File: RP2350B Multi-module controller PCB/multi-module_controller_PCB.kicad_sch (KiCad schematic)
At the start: 79 parts, among them J2 Conn_02x26_Odd_Even, J3 Conn_02x26_Odd_Even, J4 SM03B-SRSS-TB, J5 USB_C_Receptacle_USB2.0_14P, J6 USB_C_Receptacle_USB2.0_14P, J7 Module_Bay, J8 USB_A, SW1 SW_Push, SW10 BTN_MDL, SW2 SW_Push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

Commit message: all core components placed and routed
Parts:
- C11, C12, C13, C14, C15, C16, C17, C18, C2, C20, C21, C23, C8: LCSC C157353 -> (none)
- C24: LCSC C140782 -> (none)
- J2, J3: now not fitted
- J5, J6: footprint (none) -> Connector_USB:USB_C_Receptacle_G-Switch_GT-USB-7010ASV
- J7: footprint (none) -> Connector_PinHeader_2.54mm:PinHeader_1x08_P2.54mm_Vertical
- J8: footprint (none) -> Connector_USB:USB_A_Connfly_DS1095
- U1: LCSC C42415655 -> (none)
- U2: LCSC C88234 -> (none)
- U3: LCSC C97521 -> (none)
- U5: LCSC C11355 -> (none)
- U6: LCSC C144190 -> (none)
- Y1: LCSC C20625731 -> (none)
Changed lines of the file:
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@@
 			)
 		)
-		(property "LCSC" "C97521"
-			(at 60.96 90.805 0)
-			(effects
-				(font
-					(size 1.27 1.27)
-				)
-				(hide yes)
-			)
-		)
 		(pin "1"
 		)
@@
 			)
 		)
-		(property "LCSC" "C157353"
-			(at 79.121 82.0166 0)
-			(effects
-				(font
-					(size 1.27 1.27)
-				)
-				(hide yes)
-			)
-		)
 		(pin "1"
 		)
@@
 			)
 		)
-		(property "LCSC" "C157353"
-			(at 255.651 30.5816 0)
-			(effects
-				(font
-					(size 1.27 1.27)
-				)
-				(hide yes)
-			)
-		)
 		(pin "1"
 		)
@@
 			)
 		)
-		(property "LCSC" "C157353"
-			(at 267.081 30.5816 0)
-			(effects
-				(font
-					(size 1.27 1.27)
-				)
-				(hide yes)
-			)
-		)
 		(pin "1"
 		)
@@
 			)
 		)
-		(property "LCSC" "C157353"
-			(at 278.511 30.5816 0)
-			(effects
-				(font
-					(size 1.27 1.27)
-				)
-				(hide yes)
-			)
-		)
 		(pin "1"
 		)
@@
 			)
 		)
-		(property "LCSC" "C157353"
-			(at 289.941 30.5816 0)
-			(effects
-				(font
-					(size 1.27 1.27)
-				)
-				(hide yes)
-			)
-		)
 		(pin "1"
 		)
@@
 			)
 		)
-		(property "LCSC" "C157353"
-			(at 301.371 30.5816 0)
-			(effects
-				(font
-					(size 1.27 1.27)
-				)
-				(hide yes)
-			)
-		)
 		(pin "1"
 		)
@@
 			)
 		)
-		(property "LCSC" "C157353"
-			(at 312.801 30.5816 0)
-			(effects
-				(font
-					(size 1.27 1.27)
-				)
-				(hide yes)
-			)
-		)
 		(pin "1"
 		)
@@
 			)
 		)
-		(property "LCSC" "C88234"
-			(at 82.55 21.7932 0)
-			(effects
-				(font
-					(size 1.27 1.27)
-				)
-				(hide yes)
-			)
-		)
 		(pin "1"
 		)
@@
 			)
 		)
-		(property "LCSC" "C20625731"
-			(at 82.55 188.595 0)
-			(effects
-				(font
-					(size 1.27 1.27)
-				)
-				(hide yes)
-			)
-		)
 		(pin "1"
 		)
@@
 		(in_bom yes)
 		(on_board yes)
-		(dnp no)
+		(dnp yes)
 		(property "Reference" "J3"
 			(at 391.16 83.82 0)
@@
 		(in_bom yes)
 		(on_board yes)
-		(dnp no)
+		(dnp yes)
 		(property "Reference" "J2"
 			(at 334.01 83.82 0)
@@
 			)
 		)
-		(property "LCSC" "C140782"
-			(at 56.1721 257.8741 0)
-			(effects
-				(font
-					(size 1.27 1.27)
-				)
-				(hide yes)
-			)
-		)
 		(pin "1"
 		)
@@
 			)
 		)
-		(property "LCSC" "C157353"
-			(at 170.561 30.5816 0)
-			(effects
-				(font
-					(size 1.27 1.27)
-				)
-				(hide yes)
-			)
-		)
 		(pin "1"
 		)
@@
 			)
 		)
-		(property "LCSC" "C157353"
-			(at 244.221 30.5816 0)
-			(effects
-				(font
-					(size 1.27 1.27)
-				)
-				(hide yes)
-			)
-		)
 		(pin "1"
 		)
@@
 			)
 		)
-		(property "LCSC" "C11355"
-			(at 130.4133 218.1055 0)
-			(effects
-				(font
-					(size 1.27 1.27)
-				)
-				(hide yes)
-			)
-		)
 		(pin "7"
 		)
@@
 			)
 		)
-		(property "LCSC" "C157353"
-			(at 324.231 30.5816 0)
-			(effects
-				(font
-					(size 1.27 1.27)
-				)
-				(hide yes)
-			)
-		)
 		(pin "1"
 		)
@@
 			)
 		)
-		(property "LCSC" "C157353"
-			(at 50.0761 257.6201 0)
-			(effects
-				(font
-					(size 1.27 1.27)
-				)
-				(hide yes)
-			)
-		)
 		(pin "1"
 		)
@@
 			)
 		)
-		(property "Footprint" ""
+		(property "Footprint" "Connector_USB:USB_C_Receptacle_G-Switch_GT-USB-7010ASV"
 			(at 181.61 257.81 0)
 			(effects
@@
 			)
 		)
-		(property "LCSC" "C144190"
-			(at 104.14 244.7755 0)
-			(effects
-				(font
-					(size 1.27 1.27)
-				)
-				(hide yes)
-			)
-		)
 		(pin "2"
 		)
@@
 			)
 		)
-		(property "Footprint" ""
+		(property "Footprint" "Connector_PinHeader_2.54mm:PinHeader_1x08_P2.54mm_Vertical"
 			(at 25.4 262.89 0)
 			(effects
@@
 			)
 		)
-		(property "LCSC" "C157353"
-			(at 147.701 30.5816 0)
-			(effects
-				(font
-					(size 1.27 1.27)
-				)
-				(hide yes)
-			)
-		)
 		(pin "1"
 		)
@@
 			)
 		)
-		(property "LCSC" "C157353"
-			(at 232.156 30.5816 0)
-			(effects
-				(font
-					(size 1.27 1.27)
-				)
-				(hide yes)
-			)
-		)
 		(pin "1"
 		)
@@
 			)
 		)
-		(property "Footprint" ""
+		(property "Footprint" "Connector_USB:USB_A_Connfly_DS1095"
 			(at 151.13 215.9 0)
 			(effects
@@
 			)
 		)
-		(property "LCSC" "C42415655"
-			(at 201.5841 207.01 0)
-			(effects
-				(font
-					(size 1.27 1.27)
-				)
-				(hide yes)
-			)
-		)
 		(pin "1"
 		)
@@
 			)
 		)
-		(property "Footprint" ""
+		(property "Footprint" "Connector_USB:USB_C_Receptacle_G-Switch_GT-USB-7010ASV"
 			(at 33.02 38.1 0)
 			(effects

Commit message: completed layout, include production files, before adjusting component mounting
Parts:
- added J1: Conn_02x06_Odd_Even, Connector_PinSocket_2.54mm:PinSocket_2x06_P2.54mm_Vertical, symbol Connector_Generic:Conn_02x06_Odd_Even
- added J9: ADC_Breakout, Connector_JST:JST_PH_B12B-PH-K_1x12_P2.00mm_Vertical, symbol Connector_Generic:Conn_01x12
- C1, C19, C5: LCSC (none) -> C15850
- C10, C6, C7, C9: LCSC (none) -> C23733
- C11, C12, C13, C14, C15, C16, C17, C18, C2, C20, C21, C23, C25, C8: LCSC (none) -> C1525
- C24: footprint Capacitor_SMD:C_0603_1608Metric -> Capacitor_SMD:C_0805_2012Metric; LCSC (none) -> C16780
- C3, C4: LCSC (none) -> C7467172
- J4: footprint Connector_JST:JST_SH_SM03B-SRSS-TB_1x03-1MP_P1.00mm_Horizontal -> Connector_PinHeader_2.54mm:PinHeader_1x03_P2.54mm_Vertical; symbol Connector_Generic_MountingPin:Conn_01x03_MountingPin -> Connector_Generic:Conn_01x03
- J5, J6: LCSC (none) -> C2988369
- J7: LCSC (none) -> C19184340
- J8: LCSC (none) -> C456018
- L1: LCSC (none) -> C42411119
- R10: LCSC (none) -> C17168
- R12, R5: LCSC (none) -> C25905
- R14, R18: LCSC (none) -> C25744
- R15, R16: value R -> 10k; footprint (none) -> Resistor_SMD:R_0402_1005Metric; LCSC (none) -> C25744
- R17, R19: LCSC (none) -> C25792
- R2, R4, R6: LCSC (none) -> C11702
- R20: LCSC (none) -> C25130
- R21, R22: LCSC (none) -> C25104
- R23, R24: LCSC (none) -> C2906875
- R3: LCSC (none) -> C25105
- R7, R8: LCSC (none) -> C25100
- SW1, SW2: LCSC (none) -> C2910644
- SW10, SW3, SW4, SW5, SW6, SW7, SW8, SW9: LCSC (none) -> C2837532
- U1: LCSC (none) -> C42415655
- U2: LCSC (none) -> C88234
- U3: LCSC (none) -> C97521
- U5: LCSC (none) -> C11355
- U6: LCSC (none) -> C144190
- Y1: LCSC (none) -> C20625731
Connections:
- net +3V3: now also J1.10 (Pin_10), J1.12 (Pin_12), J1.8 (Pin_8), J9.1 (Pin_1)
- net GND: now also J1.1 (Pin_1), J1.11 (Pin_11), J1.3 (Pin_3), J1.5 (Pin_5), J1.7 (Pin_7), J1.9 (Pin_9), J9.3 (Pin_3), J9.4 (Pin_4); no longer J4.MP (MountPin)
- net GPIO40_ADC0: now also J9.12 (Pin_12); no longer J3.15 (Pin_15)
- net GPIO41_ADC1: now also J9.11 (Pin_11); no longer J3.13 (Pin_13)
- net GPIO42_ADC2: now also J9.10 (Pin_10); no longer J3.11 (Pin_11)
- net GPIO43_ADC3: now also J9.9 (Pin_9); no longer J3.9 (Pin_9)
- net GPIO44_ADC4: now also J9.8 (Pin_8); no longer J3.7 (Pin_7)
- net GPIO45_ADC5: now also J9.7 (Pin_7); no longer J3.5 (Pin_5)
- net GPIO46_ADC6: now also J9.6 (Pin_6); no longer J3.3 (Pin_3)
- net GPIO47_ADC7: now also J9.5 (Pin_5); no longer J3.1 (Pin_1)
- net VBUS: now also J1.2 (Pin_2), J1.4 (Pin_4), J1.6 (Pin_6), J9.2 (Pin_2)
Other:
- note added: "SWD Debug Connector"
- note removed: "JST Debug Connector"

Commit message: adjust GPIO breakout, add LED, silkscreen labels, etc
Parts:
- removed J9: ADC_Breakout, Connector_JST:JST_PH_B12B-PH-K_1x12_P2.00mm_Vertical, symbol Connector_Generic:Conn_01x12
- added D1: LED, LED_SMD:LED_0603_1608Metric, symbol Device:LED
- added J10: Internal unused GPIO Breakout, Connector_PinHeader_1.27mm:PinHeader_2x03_P1.27mm_Vertical, symbol Connector_Generic:Conn_02x03_Odd_Even
- added J9: ADC_Breakout, Connector_PinHeader_2.54mm:PinHeader_2x09_P2.54mm_Vertical, symbol Connector_Generic:Conn_02x09_Odd_Even
- added R25: 220, Resistor_SMD:R_0603_1608Metric, symbol Device:R
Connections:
- net +3V3: now also J9.1 (Pin_1)
- net GND: now also D1.1 (K), J10.1 (Pin_1), J9.3 (Pin_3), J9.4 (Pin_4)
- net GPIO17: now also J10.3 (Pin_3); no longer J2.38 (Pin_38)
- net GPIO18: now also J10.2 (Pin_2); no longer J2.40 (Pin_40)
- net GPIO19: now also J10.4 (Pin_4); no longer J2.42 (Pin_42)
- net GPIO20: now also J10.6 (Pin_6); no longer J2.44 (Pin_44)
- net GPIO21: now also J10.5 (Pin_5); no longer J2.46 (Pin_46)
- net GPIO33: now also R25.1; no longer J3.29 (Pin_29)
- net GPIO34: now also J9.17 (Pin_17); no longer J3.27 (Pin_27)
- net GPIO35: now also J9.18 (Pin_18); no longer J3.25 (Pin_25)
- net GPIO36: now also J9.15 (Pin_15); no longer J3.23 (Pin_23)
- net GPIO37: now also J9.16 (Pin_16); no longer J3.21 (Pin_21)
- net GPIO38: now also J9.13 (Pin_13); no longer J3.19 (Pin_19)
- net GPIO39: now also J9.14 (Pin_14); no longer J3.17 (Pin_17)
- net GPIO40_ADC0: now also J9.11 (Pin_11)
- net GPIO41_ADC1: now also J9.12 (Pin_12)
- net GPIO42_ADC2: now also J9.9 (Pin_9)
- net GPIO43_ADC3: now also J9.10 (Pin_10)
- net GPIO44_ADC4: now also J9.7 (Pin_7)
- net GPIO45_ADC5: now also J9.8 (Pin_8)
- net GPIO46_ADC6: now also J9.5 (Pin_5)
- net GPIO47_ADC7: now also J9.6 (Pin_6)
- net VBUS: now also J9.2 (Pin_2)
- new net: D1.2 (A), R25.2
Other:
- note added: "Status LED"
- moved on the sheet: C2, C3, C4, R1, R10, R11, R13, R2, R9, U3, Y1

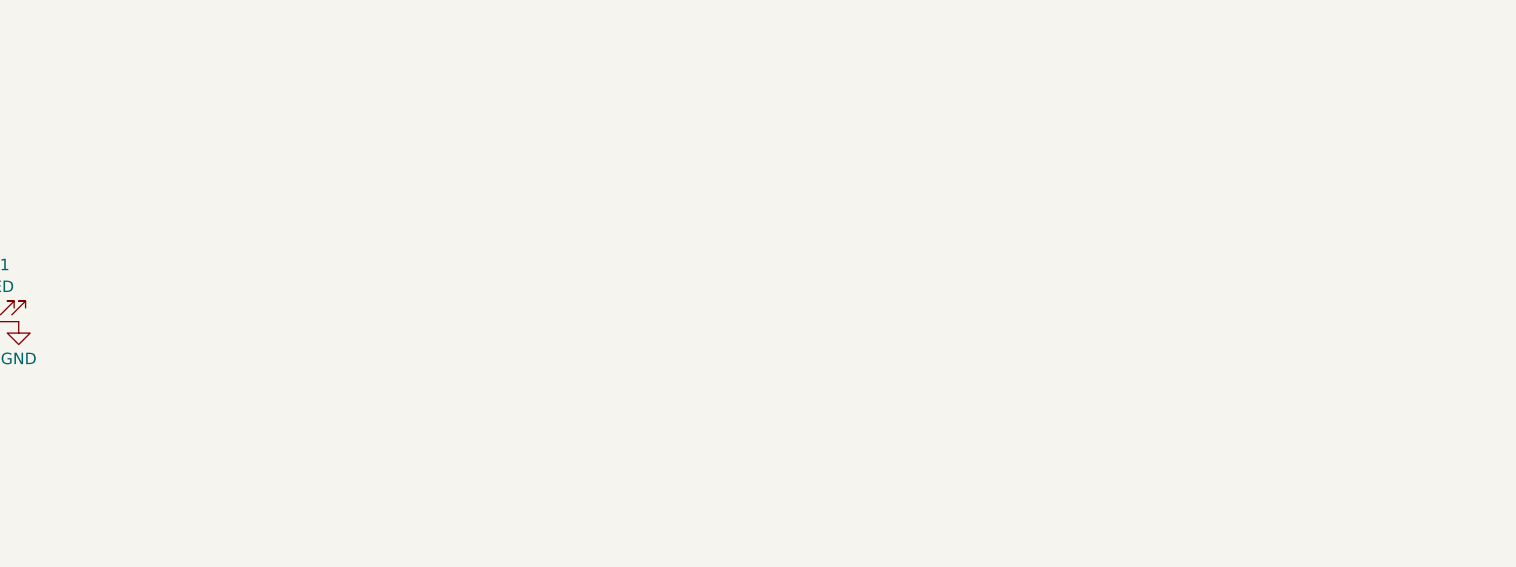
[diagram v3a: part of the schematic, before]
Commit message: add hardware tests for new board
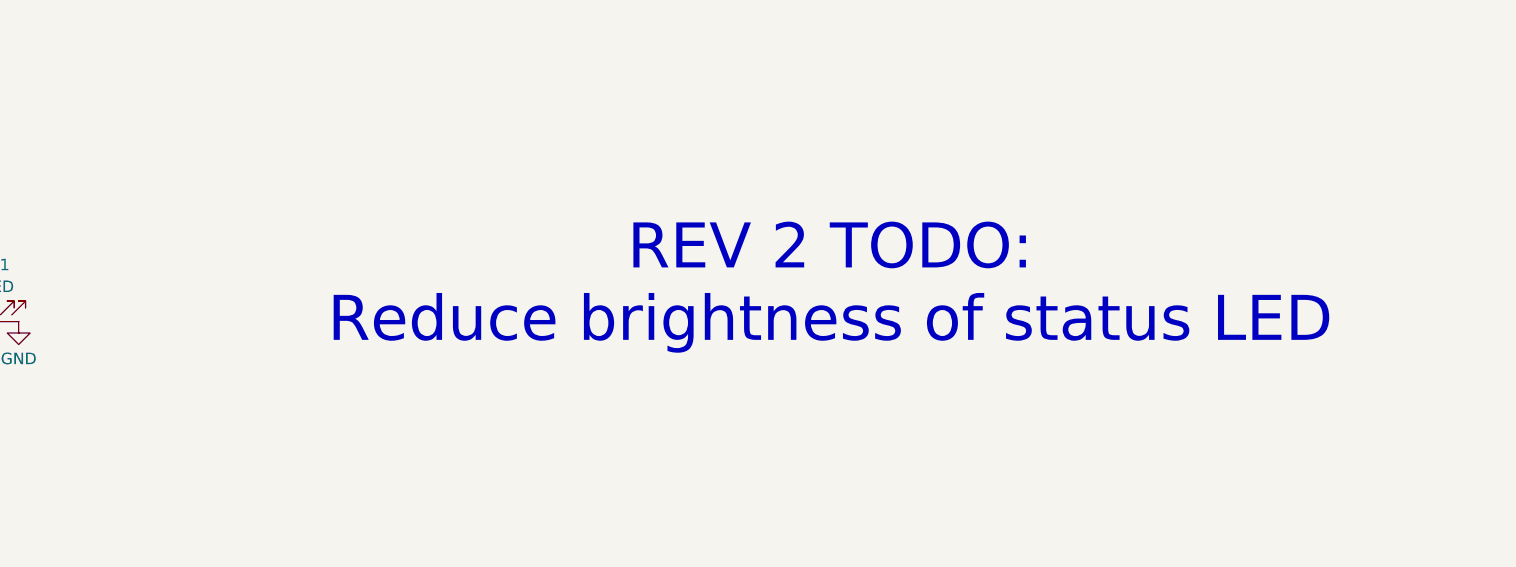
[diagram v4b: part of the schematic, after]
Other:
- note added: "REV 2 TODO: Reduce brightness of status LED"
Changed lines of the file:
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@@
+		)
+	)
+	(text "REV 2 TODO:\nReduce brightness of status LED"
+		(exclude_from_sim no)
+		(at 487.68 238.506 0)
+		(effects
+			(font
+				(size 5 5)
+			)
 		)
 	)

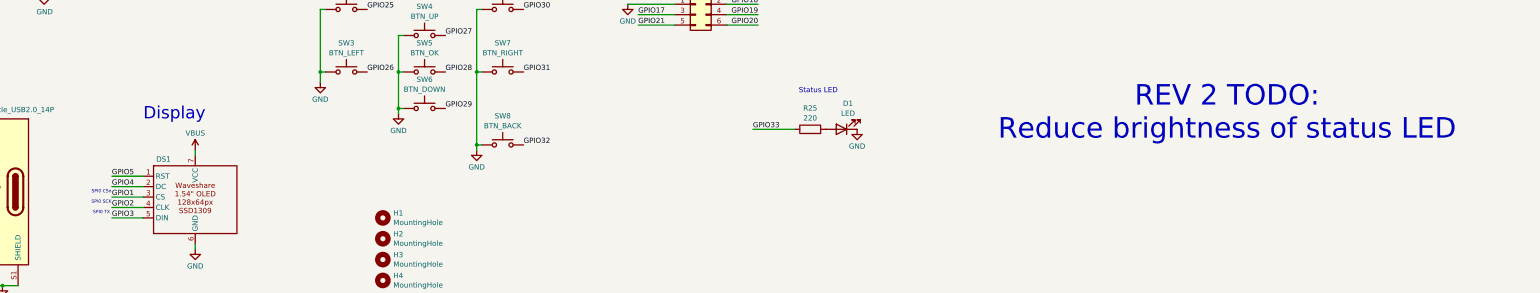
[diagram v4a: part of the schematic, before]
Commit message: Implement pin-remapping and adjustments for new PCB, add support for both USB A and C ports (configured at compile-time by active_usb_port for now). Buttons, i2c display, USB A, USB C, all functional. Multi-module adjustments WIP
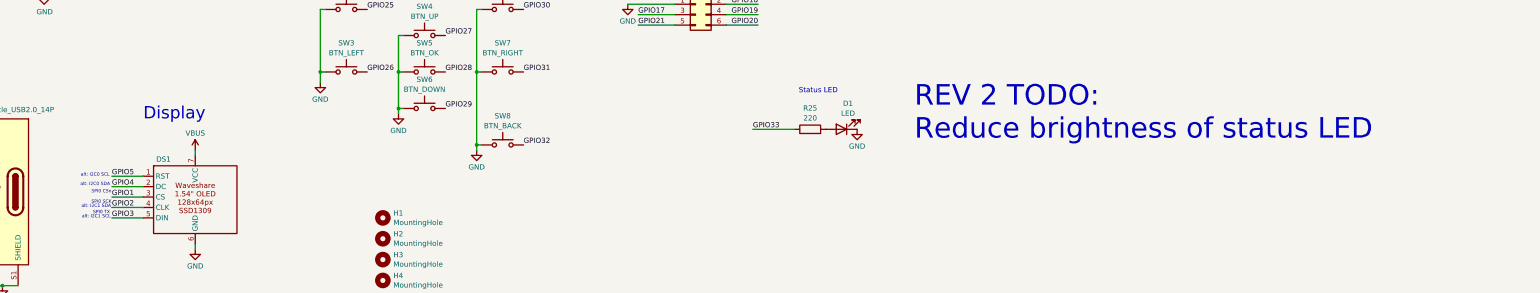
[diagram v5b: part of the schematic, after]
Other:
- note added: "alt: I2C0 SCL"
- note added: "alt: I2C0 SDA"
- note added: "alt: I2C1 SCL"
- note added: "alt: I2C1 SDA"
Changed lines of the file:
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@@
 	(text "REV 2 TODO:\nReduce brightness of status LED"
 		(exclude_from_sim no)
-		(at 487.68 238.506 0)
+		(at 411.48 238.506 0)
 		(effects
 			(font
 				(size 5 5)
 			)
+			(justify left)
 		)
 	)
@@
 		)
 	)
+	(text "alt: I2C0 SCL"
+		(exclude_from_sim no)
+		(at 211.836 253.746 0)
+		(effects
+			(font
+				(size 0.8 0.8)
+			)
+		)
+	)
 	(text "UART0 TX (CSRF)"
 		(exclude_from_sim no)
@@
 		)
 	)
+	(text "alt: I2C1 SCL"
+		(exclude_from_sim no)
+		(at 212.09 263.906 0)
+		(effects
+			(font
+				(size 0.8 0.8)
+			)
+		)
+	)
 	(text "USB Downstream ports"
 		(exclude_from_sim no)
@@
 		)
 	)
+	(text "alt: I2C0 SDA"
+		(exclude_from_sim no)
+		(at 211.836 256.032 0)
+		(effects
+			(font
+				(size 0.8 0.8)
+			)
+		)
+	)
 	(text "UART0 RX"
 		(exclude_from_sim no)
@@
 		(effects
 			(font
+				(size 0.8 0.8)
+			)
+		)
+	)
+	(text "alt: I2C1 SDA"
+		(exclude_from_sim no)
+		(at 212.09 261.366 0)
+		(effects
+			(font

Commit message: start on revisions for REV2 board design
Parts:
- added R26: 22, Resistor_SMD:R_0402_1005Metric, symbol Device:R_Small
- R20: value 680 -> 22
- R21, R22: value 330 -> 22
- R25: value 220 -> 470
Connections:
- net GPIO13: now also R26.2; no longer J7.1 (Pin_1), R20.1
- new net: J7.1 (Pin_1), R20.1, R26.1
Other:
- note added: "REV 2 Changes: Reduce R22, R21, and R20 from 330Ω (or 680Ω) to 22Ω, improving signal response time Add R26 protection resistor Increase R25 from 220Ω to 470Ω to reduce LED brightness"
- note added: "REV 2 TODO: Consider always-on power to USB C CC pins - use ADC to detect downstream devices and auto-switch active port"
- note removed: "REV 2 TODO: Reduce brightness of status LED"
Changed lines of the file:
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@@
 		(title "RP2350B QFN80 Mulit-module controller")
 		(date "2025-12-03")
-		(rev "REV1")
+		(rev "REV2")
 		(company "Patronics and Reject Robotics")
 	)
@@
 		)
 	)
-	(text "REV 2 TODO:\nReduce brightness of status LED"
+	(text "REV 2 TODO:\nConsider always-on power to USB C CC pins\n- use ADC to detect downstream devices and auto-switch active port"
 		(exclude_from_sim no)
-		(at 411.48 238.506 0)
+		(at 43.942 312.928 0)
 		(effects
 			(font
@@
 		)
 	)
+	(text "REV 2 Changes:\nReduce R22, R21, and R20 from 330Ω (or 680Ω) to 22Ω, improving signal response time\nAdd R26 protection resistor\nIncrease R25 from 220Ω to 470Ω to reduce LED brightness"
+		(exclude_from_sim no)
+		(at 40.132 348.996 0)
+		(effects
+			(font
+				(size 5 5)
+			)
+			(justify left)
+		)
+	)
 	(text "USB Downstream ports"
 		(exclude_from_sim no)
@@
 	(wire
 		(pts
-			(xy 45.72 256.54) (xy 30.48 256.54)
+			(xy 236.22 151.13) (xy 251.46 151.13)
 		)
 		(stroke
@@
 	(wire
 		(pts
-			(xy 236.22 151.13) (xy 251.46 151.13)
+			(xy 326.39 104.14) (xy 326.39 106.68)
 		)
 		(stroke
@@
 	(wire
 		(pts
-			(xy 326.39 104.14) (xy 326.39 106.68)
+			(xy 38.1 256.54) (xy 45.72 256.54)
 		)
 		(stroke
@@
 	(wire
 		(pts
+			(xy 30.48 256.54) (xy 33.02 256.54)
+		)
+		(stroke
+			(width 0)
+			(type default)
+		)
+	)
+	(wire
+		(pts
 			(xy 76.2 130.81) (xy 76.2 129.54)
 		)
@@
 			)
 		)
-		(property "Value" "330"
+		(property "Value" "22"
 			(at 35.56 265.0052 90)
 			(effects
@@
 			)
 		)
-		(property "Value" "220"
+		(property "Value" "470"
 			(at 386.08 239.8338 90)
 			(effects
@@
 			)
 		)
-		(property "Value" "330"
+		(property "Value" "22"
 			(at 35.306 261.1952 90)
 			(effects
@@
 	)
 	(symbol
+		(lib_id "Device:R_Small")
+		(at 35.56 256.54 90)
+		(unit 1)
+		(exclude_from_sim no)
+		(in_bom yes)
+		(on_board yes)
+		(dnp no)
+		(property "Reference" "R26"
+			(at 35.56 256.4353 90)
+			(effects
+				(font
+					(size 1.016 1.016)
+				)
+			)
+		)
+		(property "Value" "22"
+			(at 32.766 255.6072 90)
+			(effects
+				(font
+					(size 1.27 1.27)
+				)
+			)
+		)
+		(property "Footprint" "Resistor_SMD:R_0402_1005Metric"
+			(at 35.56 256.54 0)
+			(effects
+				(font
+					(size 1.27 1.27)
+				)
+				(hide yes)
+			)
+		)
+		(property "Datasheet" "~"
+			(at 35.56 256.54 0)
+			(effects
+				(font
+					(size 1.27 1.27)
+				)
+				(hide yes)
+			)
+		)
+		(property "Description" "Resistor, small symbol"
+			(at 35.56 256.54 0)
+			(effects
+				(font
+					(size 1.27 1.27)
+				)
+				(hide yes)
+			)
+		)
+		(property "LCSC" "C25130"
+			(at 35.56 251.8633 0)
+			(effects
+				(font
+					(size 1.27 1.27)
+				)
+				(hide yes)
+			)
+		)
+		(pin "1"
+		)
+		(pin "2"
+		)
+		(instances
+			(project "multi-module_controller_PCB"
+				(path "/94683f5c-9cd9-448e-be96-9792537b5cb8"
+					(reference "R26")
+					(unit 1)
+				)
+			)
+		)
+	)
+	(symbol
 		(lib_id "power:GND")
 		(at 321.31 40.64 0)
@@
 		(on_board yes)
 		(dnp no)
-		(fields_autoplaced yes)
 		(property "Reference" "R20"
-			(at 35.56 249.3233 90)
+			(at 35.56 253.8953 90)
 			(effects
 				(font
@@
 			)
 		)
-		(property "Value" "680"
-			(at 35.56 251.5432 90)
+		(property "Value" "22"
+			(at 35.56 252.0512 90)
 			(effects
 				(font

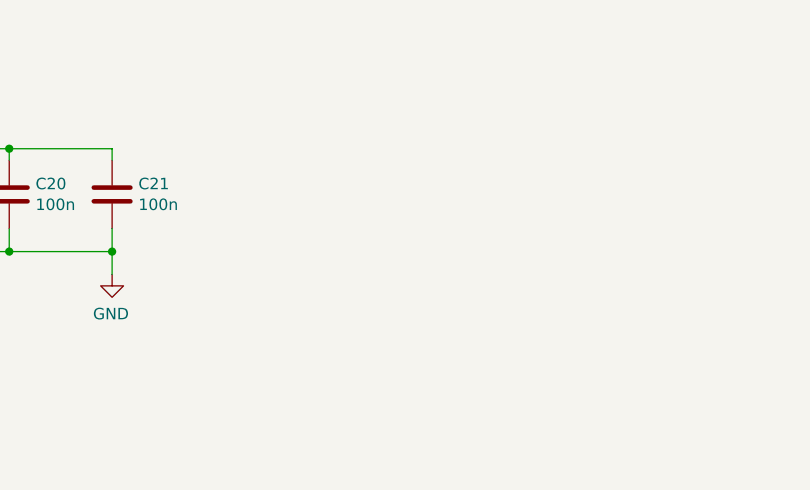
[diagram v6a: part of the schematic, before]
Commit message: Update PCB with improved bulk capacitors for VBus, increased mounting hole diameter for display, and offset multi-module connector further away from USB A port
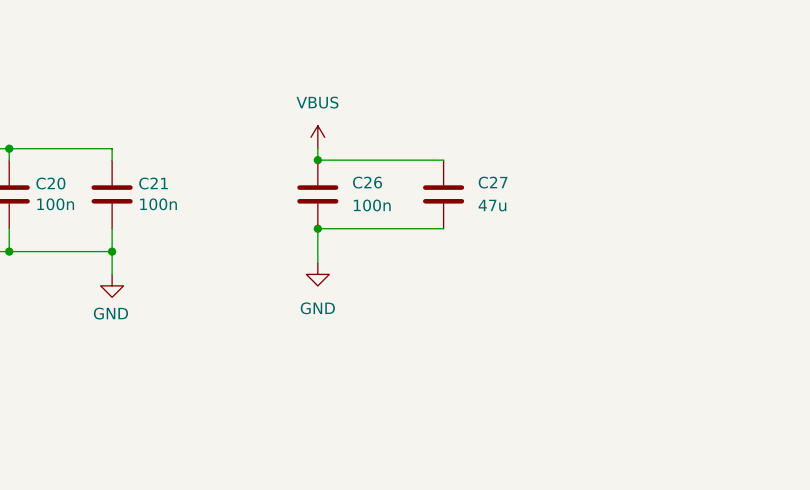
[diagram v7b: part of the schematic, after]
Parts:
- added C26: 100n, Capacitor_SMD:C_0402_1005Metric, symbol Device:C
- added C27: 47u, Capacitor_SMD:C_1206_3216Metric, symbol Device:C
- C24: footprint Capacitor_SMD:C_0805_2012Metric -> Capacitor_SMD:C_1206_3216Metric
- DS1: value ~ -> (none)
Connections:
- net GND: now also C26.2, C27.2
- net VBUS: now also C26.1, C27.1
